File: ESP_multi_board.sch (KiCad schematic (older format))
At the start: 21 parts, among them P101 CONN_01X02, P102 CONN_01X06, P103 CONN_01X02, P104 CONN_01X06, P105 CONN_01X12, P106 CONN_01X03, P107 CONN_I2C_MPU6050, P108 CONN_PINES_DIG, SW101 SW_PUSH_SMALL, SW102 SPST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

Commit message: cambio de posición ADC y L293DD
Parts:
- removed SW102: SPST, Buttons_Switches_SMD:SW_SPST_REED_CT10-XXXX-G1, symbol SPST
- added SW102: SWITCH_INV, Buttons_Switches_ThroughHole:SW_Micro_SPST, symbol SWITCH_INV
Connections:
- wire segments 83 -> 82
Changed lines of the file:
@@
 LIBS:contrib
 LIBS:valves
-LIBS:figaro
-LIBS:ADC128D818
-LIBS:sensors-cache
+LIBS:ESP8266
+LIBS:stepper drivers
+LIBS:mpu-6050
+LIBS:MCP23008
+LIBS:microchip_adcdac
+LIBS:ESP_multi_board-cache
 EELAYER 25 0
 EELAYER END
@@
 Comment4 ""
 $EndDescr
-Text GLabel 2400 900  2    60   BiDi ~ 0
+Text GLabel 2450 850  2    60   BiDi ~ 0
 VDD
 $Comp
@@
 L GND #PWR02
 U 1 1 57125BD6
-P 2450 1150
-F 0 "#PWR02" H 2450 900 50  0001 C CNN
-F 1 "GND" H 2450 1000 50  0000 C CNN
-F 2 "" H 2450 1150 50  0000 C CNN
-F 3 "" H 2450 1150 50  0000 C CNN
-	1    2450 1150
+P 1450 1200
+F 0 "#PWR02" H 1450 950 50  0001 C CNN
+F 1 "GND" H 1450 1050 50  0000 C CNN
+F 2 "" H 1450 1200 50  0000 C CNN
+F 3 "" H 1450 1200 50  0000 C CNN
+	1    1450 1200
 	0    -1   -1   0
 $EndComp
@@
 L VCC #PWR06
 U 1 1 57125BE7
-P 850 1150
-F 0 "#PWR06" H 850 1000 50  0001 C CNN
-F 1 "VCC" H 850 1300 50  0000 C CNN
-F 2 "" H 850 1150 50  0000 C CNN
-F 3 "" H 850 1150 50  0000 C CNN
-	1    850  1150
+P 900 1200
+F 0 "#PWR06" H 900 1050 50  0001 C CNN
+F 1 "VCC" H 900 1350 50  0000 C CNN
+F 2 "" H 900 1200 50  0000 C CNN
+F 3 "" H 900 1200 50  0000 C CNN
+	1    900  1200
 	0    -1   -1   0
 $EndComp
@@
 $EndComp
 $Sheet
-S 1850 750  550  600
+S 900  800  550  600
 U 57126BEE
 F0 "reg5to3_3V" 60
 F1 "reg5to3_3V.sch" 60
-F2 "GND" B R 2400 1150 60
-F3 "3_3V" B R 2400 900 60
-F4 "VCC" B L 1850 1150 60
+F2 "GND" B R 1450 1200 60
+F3 "3_3V" B R 1450 950 60
+F4 "VCC" B L 900 1200 60
 $EndSheet
 $Comp
@@
 	3850 5050 4200 5050
 Wire Wire Line
-	4200 5050 4200 5450
-Wire Wire Line
-	4200 5450 4450 5450
+	4200 5050 4200 5850
 Wire Wire Line
 	3850 5150 4150 5150
@@
 	4150 5150 4150 5650
 Wire Wire Line
-	4150 5650 4450 5650
-Wire Wire Line
 	3850 5250 4100 5250
 Wire Wire Line
-	4100 5250 4100 5850
-Wire Wire Line
-	4100 5850 4450 5850
+	4100 5250 4100 5450
 Wire Wire Line
 	3850 5350 4050 5350
@@
 	4050 6200 6350 6200
 Wire Wire Line
-	6350 6200 6350 5250
+	6350 6200 6350 5850
 Wire Wire Line
 	3850 5450 4000 5450
@@
 	4000 6250 6400 6250
 Wire Wire Line
-	6400 6250 6400 5450
+	6400 6250 6400 5650
 Wire Wire Line
 	3950 5550 3950 6300
@@
 	3950 6300 6450 6300
 Wire Wire Line
-	6450 6300 6450 5650
-Wire Wire Line
-	6500 5850 6500 6350
+	6450 6300 6450 5450
+Wire Wire Line
+	6500 5250 6500 6350
 Wire Wire Line
 	6500 6350 3900 6350
@@
 Connection ~ 5900 1150
 Connection ~ 6100 1250
-Wire Wire Line
-	2400 1150 2450 1150
 Wire Wire Line
 	7500 3050 7500 3150
@@
 	1400 4850 1250 4850
 Connection ~ 1250 4850
-Wire Wire Line
-	6350 5250 6200 5250
-Wire Wire Line
-	6400 5450 6200 5450
-Wire Wire Line
-	6450 5650 6200 5650
-Wire Wire Line
-	6500 5850 6200 5850
 $Comp
 L PWR_FLAG #FLG018
@@
 NoConn ~ 7750 2050
 $Comp
-L SPST SW102
-U 1 1 57214B62
-P 1350 1150
-F 0 "SW102" H 1350 1250 50  0000 C CNN
-F 1 "SPST" H 1350 1050 50  0000 C CNN
-F 2 "Buttons_Switches_SMD:SW_SPST_REED_CT10-XXXX-G1" H 1350 1150 50  0001 C CNN
-F 3 "" H 1350 1150 50  0000 C CNN
-	1    1350 1150
-	1    0    0    -1
-$EndComp
+L SWITCH_INV SW102
+U 1 1 57214298
+P 1950 950
+F 0 "SW102" H 1750 1100 50  0000 C CNN
+F 1 "SWITCH_INV" H 1800 800 50  0000 C CNN
+F 2 "Buttons_Switches_ThroughHole:SW_Micro_SPST" H 1950 950 50  0001 C CNN
+F 3 "" H 1950 950 50  0000 C CNN
+	1    1950 950
+	1    0    0    -1
+$EndComp
+Wire Wire Line
+	6500 5250 6200 5250
+Wire Wire Line
+	6450 5450 6200 5450
+Wire Wire Line
+	6400 5650 6200 5650
+Wire Wire Line
+	6350 5850 6200 5850
+Wire Wire Line
+	4100 5450 4450 5450
+Wire Wire Line
+	4150 5650 4450 5650
+Wire Wire Line
+	4200 5850 4450 5850
 $EndSCHEMATC

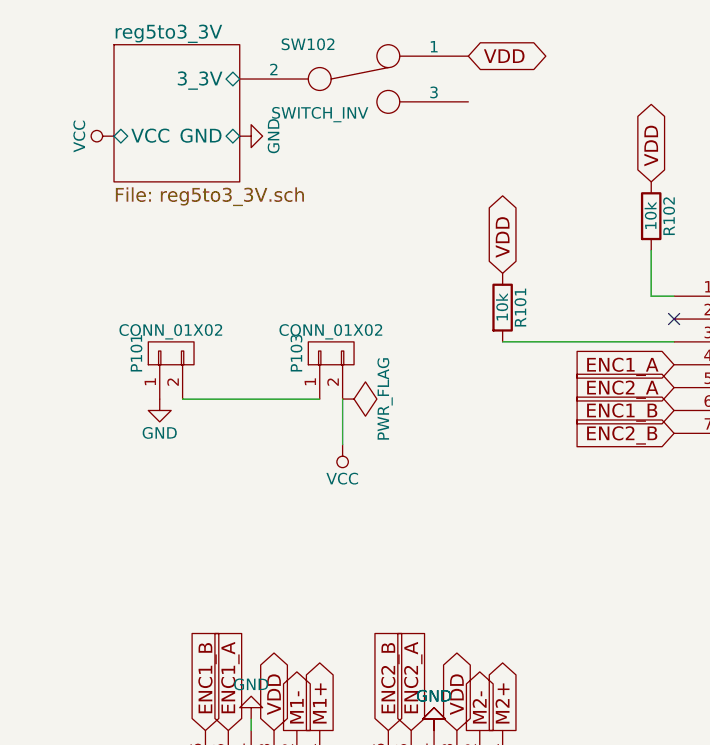
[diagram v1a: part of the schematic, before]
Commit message: incluida version de la placa alargada 10x2.5 cm
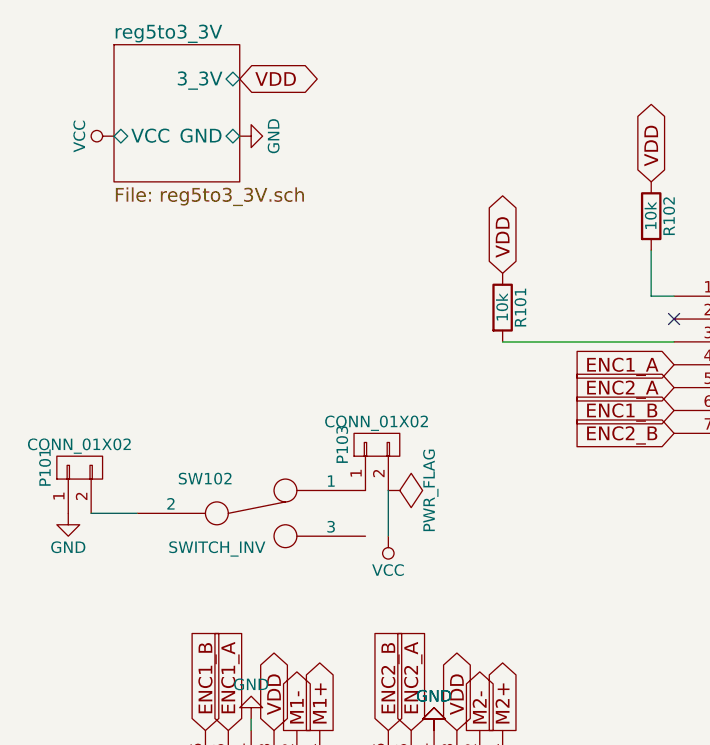
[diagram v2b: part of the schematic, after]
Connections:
- net VDD: no longer SW102.1
- net at P103.1 (P1): now also SW102.1; no longer P101.2 (P2)
- net reg5to3_3V/3_3V: no longer names the net of SW102.2
- net reg5to3_3V/3_3V: now also P101.2 (P2)
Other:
- moved on the sheet: P101, P103, SW102
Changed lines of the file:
@@
 Comment4 ""
 $EndDescr
-Text GLabel 2450 850  2    60   BiDi ~ 0
+Text GLabel 1450 950  2    60   BiDi ~ 0
 VDD
 $Comp
@@
 L CONN_01X02 P103
 U 1 1 57125BEB
-P 1850 2150
-F 0 "P103" H 1850 2300 50  0000 C CNN
-F 1 "CONN_01X02" V 1950 2150 50  0000 C CNN
-F 2 "Pin_Headers:Pin_Header_Angled_1x02" H 1850 2150 50  0001 C CNN
-F 3 "" H 1850 2150 50  0000 C CNN
-	1    1850 2150
+P 2050 2550
+F 0 "P103" H 2050 2700 50  0000 C CNN
+F 1 "CONN_01X02" V 2150 2550 50  0000 C CNN
+F 2 "Pin_Headers:Pin_Header_Angled_1x02" H 2050 2550 50  0001 C CNN
+F 3 "" H 2050 2550 50  0000 C CNN
+	1    2050 2550
 	0    -1   -1   0
 $EndComp
@@
 L CONN_01X02 P101
 U 1 1 57125BEC
-P 1150 2150
-F 0 "P101" H 1150 2300 50  0000 C CNN
-F 1 "CONN_01X02" V 1250 2150 50  0000 C CNN
-F 2 "Pin_Headers:Pin_Header_Angled_1x02" H 1150 2150 50  0001 C CNN
-F 3 "" H 1150 2150 50  0000 C CNN
-	1    1150 2150
+P 750 2650
+F 0 "P101" H 750 2800 50  0000 C CNN
+F 1 "CONN_01X02" V 850 2650 50  0000 C CNN
+F 2 "Pin_Headers:Pin_Header_Angled_1x02" H 750 2650 50  0001 C CNN
+F 3 "" H 750 2650 50  0000 C CNN
+	1    750  2650
 	0    -1   -1   0
 $EndComp
@@
 L GND #PWR09
 U 1 1 57125BEE
-P 1100 2350
-F 0 "#PWR09" H 1100 2100 50  0001 C CNN
-F 1 "GND" H 1100 2200 50  0000 C CNN
-F 2 "" H 1100 2350 50  0000 C CNN
-F 3 "" H 1100 2350 50  0000 C CNN
-	1    1100 2350
+P 700 2850
+F 0 "#PWR09" H 700 2600 50  0001 C CNN
+F 1 "GND" H 700 2700 50  0000 C CNN
+F 2 "" H 700 2850 50  0000 C CNN
+F 3 "" H 700 2850 50  0000 C CNN
+	1    700  2850
 	1    0    0    -1
 $EndComp
@@
 	1    0    0    -1
 $EndComp
-Wire Wire Line
-	3950 4450 4450 4450
-Wire Wire Line
-	3950 4450 3950 4550
-Wire Wire Line
-	3850 4650 4450 4650
-Wire Wire Line
-	4450 4850 4350 4850
-Wire Wire Line
-	4350 4850 4350 4750
-Wire Wire Line
-	4350 4750 3850 4750
-Wire Wire Line
-	4450 5050 4300 5050
-Wire Wire Line
-	4300 5050 4300 4850
-Wire Wire Line
-	4300 4850 3850 4850
-Wire Wire Line
-	3850 4950 4250 4950
-Wire Wire Line
-	4250 4950 4250 5250
-Wire Wire Line
-	4250 5250 4450 5250
-Wire Wire Line
-	3850 5050 4200 5050
-Wire Wire Line
-	4200 5050 4200 5850
-Wire Wire Line
-	3850 5150 4150 5150
-Wire Wire Line
-	4150 5150 4150 5650
-Wire Wire Line
-	3850 5250 4100 5250
-Wire Wire Line
-	4100 5250 4100 5450
-Wire Wire Line
-	3850 5350 4050 5350
-Wire Wire Line
-	4050 5350 4050 6200
-Wire Wire Line
-	4050 6200 6350 6200
-Wire Wire Line
-	6350 6200 6350 5850
-Wire Wire Line
-	3850 5450 4000 5450
-Wire Wire Line
-	4000 5450 4000 6250
-Wire Wire Line
-	4000 6250 6400 6250
-Wire Wire Line
-	6400 6250 6400 5650
-Wire Wire Line
-	3950 5550 3950 6300
-Wire Wire Line
-	3950 6300 6450 6300
-Wire Wire Line
-	6450 6300 6450 5450
-Wire Wire Line
-	6500 5250 6500 6350
-Wire Wire Line
-	6500 6350 3900 6350
-Wire Wire Line
-	3900 6350 3900 5650
-Wire Wire Line
-	3900 5650 3850 5650
-Wire Wire Line
-	3950 5550 3850 5550
-Wire Wire Line
-	3950 4550 3850 4550
-Wire Wire Line
-	9150 1950 9700 1950
-Wire Wire Line
-	9900 1850 9150 1850
-Wire Wire Line
-	9150 1750 10200 1750
-Wire Wire Line
-	10200 1650 9150 1650
-Wire Wire Line
-	9150 1550 10200 1550
-Wire Wire Line
-	10200 1450 9150 1450
-Wire Wire Line
-	1200 2350 1800 2350
-Wire Wire Line
-	3250 1700 3250 1900
-Wire Wire Line
-	3250 1900 3350 1900
-Wire Wire Line
-	2600 2100 3350 2100
-Wire Wire Line
-	5700 1250 6100 1250
-Wire Wire Line
-	6100 1250 6100 1350
-Wire Wire Line
-	5700 1150 5900 1150
-Wire Wire Line
-	5900 1150 5900 1300
-Connection ~ 5900 1150
-Connection ~ 6100 1250
-Wire Wire Line
-	7500 3050 7500 3150
-Wire Wire Line
-	1500 3750 1500 3800
-Wire Wire Line
-	4250 3100 4250 3150
-Wire Wire Line
-	7750 1650 7700 1650
-Wire Wire Line
-	7700 1650 7700 1750
-Wire Wire Line
-	7700 1750 7750 1750
-Connection ~ 7700 1700
-Wire Wire Line
-	7000 3100 7000 3150
-Wire Wire Line
-	9150 2150 9300 2150
-Wire Wire Line
-	9150 2050 9500 2050
-Wire Wire Line
-	5250 2000 5150 2000
-Wire Wire Line
-	5250 1900 5150 1900
-Wire Wire Line
-	2500 4650 2650 4650
-Wire Wire Line
-	2650 4650 2650 4950
-Wire Wire Line
-	2650 4950 2500 4950
-Wire Wire Line
-	2500 4850 2650 4850
-Connection ~ 2650 4850
-Wire Wire Line
-	2500 4750 2650 4750
-Connection ~ 2650 4750
-Wire Wire Line
-	2650 4800 2750 4800
-Connection ~ 2650 4800
 $Comp
 L GND #PWR016
@@
 Text GLabel 1400 4350 0    60   Input ~ 0
 EN1
-Wire Wire Line
-	1250 4950 1400 4950
-Wire Wire Line
-	1250 4650 1250 4950
-Wire Wire Line
-	1250 4650 1400 4650
-Wire Wire Line
-	950  4750 1400 4750
-Connection ~ 1250 4750
-Wire Wire Line
-	1400 4850 1250 4850
-Connection ~ 1250 4850
 $Comp
 L PWR_FLAG #FLG018
 U 1 1 57154A7C
-P 1900 2350
-F 0 "#FLG018" H 1900 2445 50  0001 C CNN
-F 1 "PWR_FLAG" H 1900 2530 50  0000 C CNN
-F 2 "" H 1900 2350 50  0000 C CNN
-F 3 "" H 1900 2350 50  0000 C CNN
-	1    1900 2350
+P 2100 2750
+F 0 "#FLG018" H 2100 2845 50  0001 C CNN
+F 1 "PWR_FLAG" H 2100 2930 50  0000 C CNN
+F 2 "" H 2100 2750 50  0000 C CNN
+F 3 "" H 2100 2750 50  0000 C CNN
+	1    2100 2750
 	0    1    1    0
 $EndComp
@@
 L VCC #PWR019
 U 1 1 57154E13
-P 1900 2550
-F 0 "#PWR019" H 1900 2400 50  0001 C CNN
-F 1 "VCC" H 1900 2700 50  0000 C CNN
-F 2 "" H 1900 2550 50  0000 C CNN
-F 3 "" H 1900 2550 50  0000 C CNN
-	1    1900 2550
+P 2100 2950
+F 0 "#PWR019" H 2100 2800 50  0001 C CNN
+F 1 "VCC" H 2100 3100 50  0000 C CNN
+F 2 "" H 2100 2950 50  0000 C CNN
+F 3 "" H 2100 2950 50  0000 C CNN
+	1    2100 2950
 	-1   0    0    1
 $EndComp
-Wire Wire Line
-	1900 2350 1900 2550
 $Comp
 L PWR_FLAG #FLG020
@@
 	1    0    0    -1
 $EndComp
-Connection ~ 6750 1650
-Wire Wire Line
-	6750 1400 6750 1800
 Text GLabel 6450 1150 1    60   BiDi ~ 0
 VDD
-Connection ~ 6450 1400
-Connection ~ 6450 1650
 $Comp
 L CP C101
@@
 	0    1    1    0
 $EndComp
-Wire Wire Line
-	6450 1150 6450 1650
-Wire Wire Line
-	5150 2300 5950 2300
 $Comp
 L SW_PUSH_SMALL SW101
@@
 Text GLabel 5950 2300 2    60   BiDi ~ 0
 SCL
-Connection ~ 5800 2300
 NoConn ~ 7600 3150
 NoConn ~ 7750 2050
@@
 L SWITCH_INV SW102
 U 1 1 57214298
-P 1950 950
-F 0 "SW102" H 1750 1100 50  0000 C CNN
-F 1 "SWITCH_INV" H 1800 800 50  0000 C CNN
-F 2 "Buttons_Switches_ThroughHole:SW_Micro_SPST" H 1950 950 50  0001 C CNN
-F 3 "" H 1950 950 50  0000 C CNN
-	1    1950 950
-	1    0    0    -1
-$EndComp
+P 1500 2850
+F 0 "SW102" H 1300 3000 50  0000 C CNN
+F 1 "SWITCH_INV" H 1350 2700 50  0000 C CNN
+F 2 "Buttons_Switches_ThroughHole:SW_Micro_SPST" H 1500 2850 50  0001 C CNN
+F 3 "" H 1500 2850 50  0000 C CNN
+	1    1500 2850
+	1    0    0    -1
+$EndComp
+Wire Wire Line
+	3950 4450 4450 4450
+Wire Wire Line
+	3950 4450 3950 4550
+Wire Wire Line
+	3850 4650 4450 4650
+Wire Wire Line
+	4450 4850 4350 4850
+Wire Wire Line
+	4350 4850 4350 4750
+Wire Wire Line
+	4350 4750 3850 4750
+Wire Wire Line
+	4450 5050 4300 5050
+Wire Wire Line
+	4300 5050 4300 4850
+Wire Wire Line
+	4300 4850 3850 4850
+Wire Wire Line
+	3850 4950 4250 4950
+Wire Wire Line
+	4250 4950 4250 5250
+Wire Wire Line
+	4250 5250 4450 5250
+Wire Wire Line
+	3850 5050 4200 5050
+Wire Wire Line
+	4200 5050 4200 5850
+Wire Wire Line
+	3850 5150 4150 5150
+Wire Wire Line
+	4150 5150 4150 5650
+Wire Wire Line
+	3850 5250 4100 5250
+Wire Wire Line
+	4100 5250 4100 5450
+Wire Wire Line
+	3850 5350 4050 5350
+Wire Wire Line
+	4050 5350 4050 6200
+Wire Wire Line
+	4050 6200 6350 6200
+Wire Wire Line
+	6350 6200 6350 5850
+Wire Wire Line
+	3850 5450 4000 5450
+Wire Wire Line
+	4000 5450 4000 6250
+Wire Wire Line
+	4000 6250 6400 6250
+Wire Wire Line
+	6400 6250 6400 5650
+Wire Wire Line
+	3950 5550 3950 6300
+Wire Wire Line
+	3950 6300 6450 6300
+Wire Wire Line
+	6450 6300 6450 5450
+Wire Wire Line
+	6500 5250 6500 6350
+Wire Wire Line
+	6500 6350 3900 6350
+Wire Wire Line
+	3900 6350 3900 5650
+Wire Wire Line
+	3900 5650 3850 5650
+Wire Wire Line
+	3950 5550 3850 5550
+Wire Wire Line
+	3950 4550 3850 4550
+Wire Wire Line
+	9150 1950 9700 1950
+Wire Wire Line
+	9900 1850 9150 1850
+Wire Wire Line
+	9150 1750 10200 1750
+Wire Wire Line
+	10200 1650 9150 1650
+Wire Wire Line
+	9150 1550 10200 1550
+Wire Wire Line
+	10200 1450 9150 1450
+Wire Wire Line
+	800  2850 1000 2850
+Wire Wire Line
+	3250 1700 3250 1900
+Wire Wire Line
+	3250 1900 3350 1900
+Wire Wire Line
+	2600 2100 3350 2100
+Wire Wire Line
+	5700 1250 6100 1250
+Wire Wire Line
+	6100 1250 6100 1350
+Wire Wire Line
+	5700 1150 5900 1150
+Wire Wire Line
+	5900 1150 5900 1300
+Connection ~ 5900 1150
+Connection ~ 6100 1250
+Wire Wire Line
+	7500 3050 7500 3150
+Wire Wire Line
+	1500 3750 1500 3800
+Wire Wire Line
+	4250 3100 4250 3150
+Wire Wire Line
+	7750 1650 7700 1650
+Wire Wire Line
+	7700 1650 7700 1750
+Wire Wire Line
+	7700 1750 7750 1750
+Connection ~ 7700 1700
+Wire Wire Line
+	7000 3100 7000 3150
+Wire Wire Line
+	9150 2150 9300 2150
+Wire Wire Line
+	9150 2050 9500 2050
+Wire Wire Line
+	5250 2000 5150 2000
+Wire Wire Line
+	5250 1900 5150 1900
+Wire Wire Line
+	2500 4650 2650 4650
+Wire Wire Line
+	2650 4650 2650 4950
+Wire Wire Line
+	2650 4950 2500 4950
+Wire Wire Line
+	2500 4850 2650 4850
+Connection ~ 2650 4850
+Wire Wire Line
+	2500 4750 2650 4750
+Connection ~ 2650 4750
+Wire Wire Line
+	2650 4800 2750 4800
+Connection ~ 2650 4800
+Wire Wire Line
+	1250 4950 1400 4950
+Wire Wire Line
+	1250 4650 1250 4950
+Wire Wire Line
+	1250 4650 1400 4650
+Wire Wire Line
+	950  4750 1400 4750
+Connection ~ 1250 4750
+Wire Wire Line
+	1400 4850 1250 4850
+Connection ~ 1250 4850
+Wire Wire Line
+	2100 2750 2100 2950
+Connection ~ 6750 1650
+Wire Wire Line
+	6750 1400 6750 1800
+Connection ~ 6450 1400
+Connection ~ 6450 1650
+Wire Wire Line
+	6450 1150 6450 1650
+Wire Wire Line
+	5150 2300 5950 2300
+Connection ~ 5800 2300
 Wire Wire Line
 	6500 5250 6200 5250

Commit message: routing
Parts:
- added D101: D, Diodes_ThroughHole:Diode_DO-35_SOD27_Horizontal_RM10, symbol D
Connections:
- net at P101.2 (P2): now also D101.1 (K); no longer SW102.2
- new net: D101.2 (A), SW102.2
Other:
- moved on the sheet: P103, SW102
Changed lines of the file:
@@
 L CONN_01X02 P103
 U 1 1 57125BEB
-P 2050 2550
-F 0 "P103" H 2050 2700 50  0000 C CNN
-F 1 "CONN_01X02" V 2150 2550 50  0000 C CNN
-F 2 "Pin_Headers:Pin_Header_Angled_1x02" H 2050 2550 50  0001 C CNN
-F 3 "" H 2050 2550 50  0000 C CNN
-	1    2050 2550
+P 2400 2550
+F 0 "P103" H 2400 2700 50  0000 C CNN
+F 1 "CONN_01X02" V 2500 2550 50  0000 C CNN
+F 2 "Pin_Headers:Pin_Header_Angled_1x02" H 2400 2550 50  0001 C CNN
+F 3 "" H 2400 2550 50  0000 C CNN
+	1    2400 2550
 	0    -1   -1   0
 $EndComp
@@
 L PWR_FLAG #FLG018
 U 1 1 57154A7C
-P 2100 2750
-F 0 "#FLG018" H 2100 2845 50  0001 C CNN
-F 1 "PWR_FLAG" H 2100 2930 50  0000 C CNN
-F 2 "" H 2100 2750 50  0000 C CNN
-F 3 "" H 2100 2750 50  0000 C CNN
-	1    2100 2750
+P 2450 2750
+F 0 "#FLG018" H 2450 2845 50  0001 C CNN
+F 1 "PWR_FLAG" H 2450 2930 50  0000 C CNN
+F 2 "" H 2450 2750 50  0000 C CNN
+F 3 "" H 2450 2750 50  0000 C CNN
+	1    2450 2750
 	0    1    1    0
 $EndComp
@@
 L VCC #PWR019
 U 1 1 57154E13
-P 2100 2950
-F 0 "#PWR019" H 2100 2800 50  0001 C CNN
-F 1 "VCC" H 2100 3100 50  0000 C CNN
-F 2 "" H 2100 2950 50  0000 C CNN
-F 3 "" H 2100 2950 50  0000 C CNN
-	1    2100 2950
+P 2450 2950
+F 0 "#PWR019" H 2450 2800 50  0001 C CNN
+F 1 "VCC" H 2450 3100 50  0000 C CNN
+F 2 "" H 2450 2950 50  0000 C CNN
+F 3 "" H 2450 2950 50  0000 C CNN
+	1    2450 2950
 	-1   0    0    1
 $EndComp
@@
 L SWITCH_INV SW102
 U 1 1 57214298
-P 1500 2850
-F 0 "SW102" H 1300 3000 50  0000 C CNN
-F 1 "SWITCH_INV" H 1350 2700 50  0000 C CNN
-F 2 "Buttons_Switches_ThroughHole:SW_Micro_SPST" H 1500 2850 50  0001 C CNN
-F 3 "" H 1500 2850 50  0000 C CNN
-	1    1500 2850
+P 1850 2850
+F 0 "SW102" H 1650 3000 50  0000 C CNN
+F 1 "SWITCH_INV" H 1700 2700 50  0000 C CNN
+F 2 "Buttons_Switches_ThroughHole:SW_Micro_SPST" H 1850 2850 50  0001 C CNN
+F 3 "" H 1850 2850 50  0000 C CNN
+	1    1850 2850
 	1    0    0    -1
 $EndComp
@@
 Connection ~ 1250 4850
 Wire Wire Line
-	2100 2750 2100 2950
+	2450 2750 2450 2950
 Connection ~ 6750 1650
 Wire Wire Line
@@
 Wire Wire Line
 	4200 5850 4450 5850
+$Comp
+L D D101
+U 1 1 57231093
+P 1150 2850
+F 0 "D101" H 1150 2950 50  0000 C CNN
+F 1 "D" H 1150 2750 50  0000 C CNN
+F 2 "Diodes_ThroughHole:Diode_DO-35_SOD27_Horizontal_RM10" H 1150 2850 50  0001 C CNN
+F 3 "" H 1150 2850 50  0000 C CNN
+	1    1150 2850
+	1    0    0    -1
+$EndComp
+Wire Wire Line
+	1350 2850 1300 2850
 $EndSCHEMATC

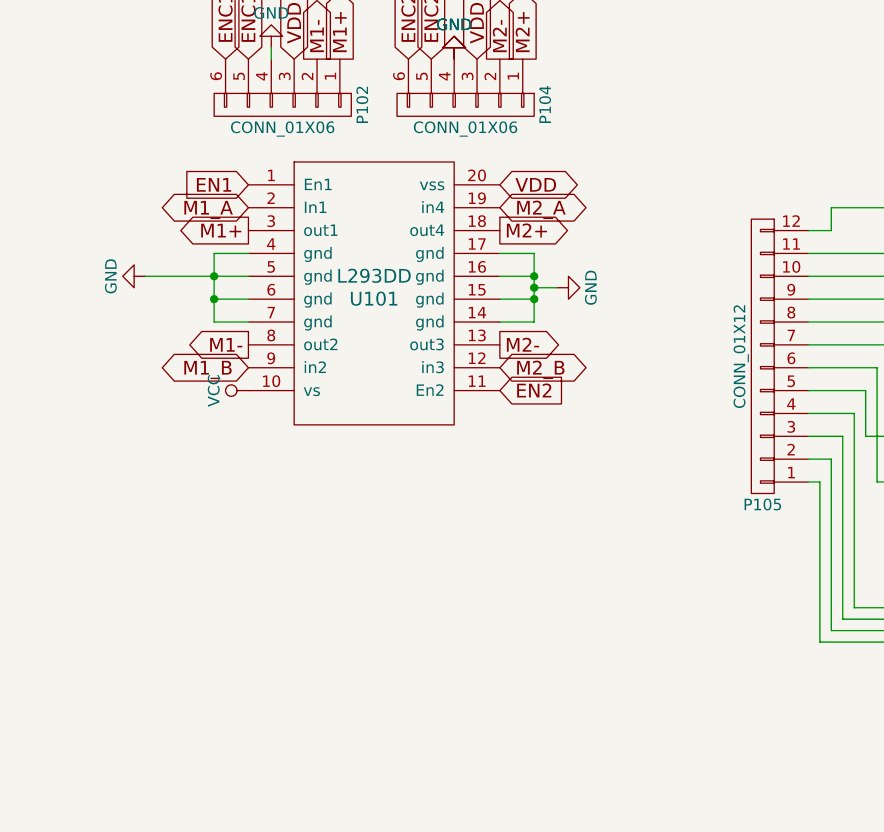
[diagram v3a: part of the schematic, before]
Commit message: cambio a L298 con diodos
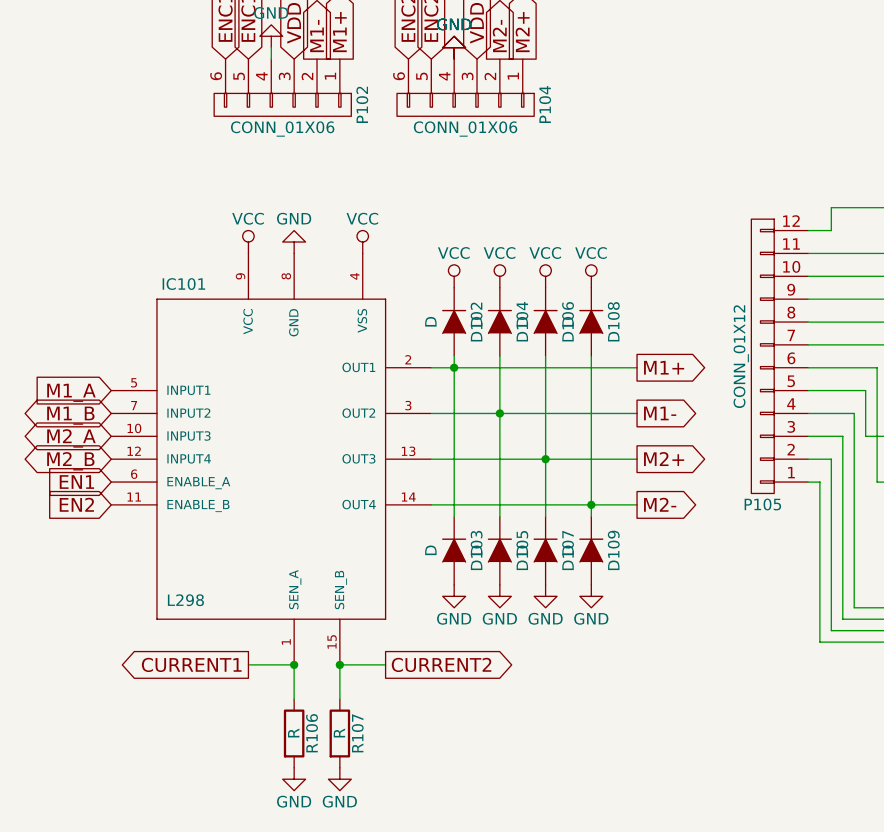
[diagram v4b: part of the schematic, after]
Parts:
- removed U101: L293DD, Housings_SOIC:SOIC-20_7.5x12.8mm_Pitch1.27mm, symbol L293DD
- added D102, D103, D104, D105, D106, D107, D108, D109: D, symbol D
- added IC101: L298, TO_SOT_Packages_THT:Multiwatt_15_Vertical, symbol L298
- added R106, R107: R, symbol R
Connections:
- net EN1: now also IC101.6 (ENABLE_A)
- net EN2: now also IC101.11 (ENABLE_B)
- net GND: now also D103.2 (A), D105.2 (A), D107.2 (A), D109.2 (A), IC101.8 (GND), R106.2, R107.2
- net M1+: now also D102.2 (A), D103.1 (K), IC101.2 (OUT1)
- net M1-: now also D104.2 (A), D105.1 (K), IC101.3 (OUT2)
- net M1_A: now also IC101.5 (INPUT1)
- net M1_B: now also IC101.7 (INPUT2)
- net M2+: now also D106.2 (A), D107.1 (K), IC101.13 (OUT3)
- net M2-: now also D108.2 (A), D109.1 (K), IC101.14 (OUT4)
- net M2_A: now also IC101.10 (INPUT3)
- net M2_B: now also IC101.12 (INPUT4)
- net VCC: now also D102.1 (K), D104.1 (K), D106.1 (K), D108.1 (K), IC101.4 (VSS), IC101.9 (VCC)
- new net CURRENT1: IC101.1 (SEN_A), R106.1
- new net CURRENT2: IC101.15 (SEN_B), R107.1
